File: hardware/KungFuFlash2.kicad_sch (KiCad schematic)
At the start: 52 parts, among them J1 SWD, J2 USB_B_Micro, J3 Wifi, Q1 BC817, SW1 Reset, SW2 Menu, SW3 Special, U1 C64-Exp-Port, U2 AMS1117-3.3, U3 STM32H7B0VBTx, Y1 25MHz

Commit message: Add USB C and JLCPCB files
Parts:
- removed J2: USB_B_Micro, KungFuFlash2:Conn_USBmicro-B_ebay-side_TH, symbol KungFuFlash2:USB_B_Micro-Connector
- removed Y1: 25MHz, Crystal:Crystal_SMD_5032-2Pin_5.0x3.2mm, symbol Device:Crystal
- added J4: USB_C_Receptacle_USB2.0, Connector_USB:USB_C_Receptacle_XKB_U262-16XN-4BVC11, symbol Connector:USB_C_Receptacle_USB2.0
- added R16, R17: 10k, Resistor_SMD:R_0805_2012Metric_Pad1.20x1.40mm_HandSolder, symbol Device:R
- added Y1: 25 MHz, Crystal:Crystal_SMD_3225-4Pin_3.2x2.5mm, symbol Device:Crystal_GND24
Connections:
- net +5C: now also J4.A4 (VBUS), J4.A9 (VBUS), J4.B4 (VBUS), J4.B9 (VBUS)
- net GND: now also J4.A1 (GND), J4.A12 (GND), J4.B1 (GND), J4.B12 (GND), J4.S1 (SHIELD), R16.1, R17.1, Y1.2, Y1.4
- net USB_DM: now also J4.A7 (D-), J4.B7 (D-)
- net USB_DP: now also J4.A6 (D+), J4.B6 (D+)
- net at C7.2, U3.12 (PH0): now also Y1.3
- net at C8.2, U3.13 (PH1): now also Y1.1
- new net: J4.B5 (CC2), R16.2
- new net: J4.A5 (CC1), R17.2
- no-connect marks 26 -> 25
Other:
- moved on the sheet: C7, C8

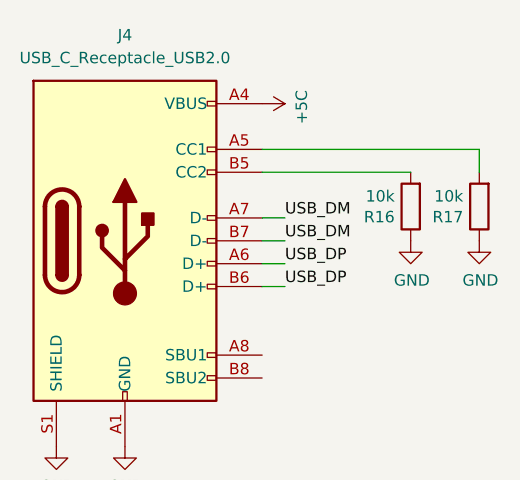
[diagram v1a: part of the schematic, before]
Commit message: Update PCB for USBC resistors 5.1k and production files
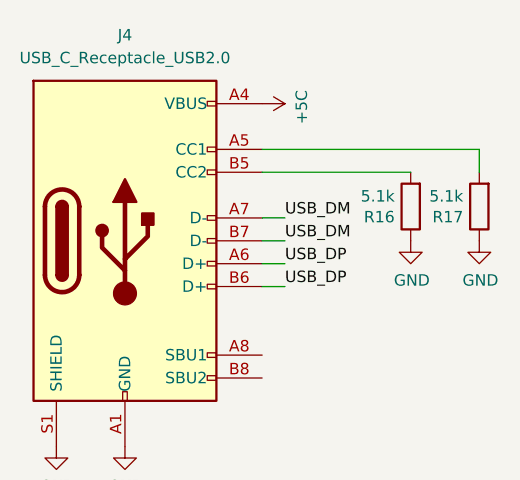
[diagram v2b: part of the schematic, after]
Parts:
- R16, R17: value 10k -> 5.1k
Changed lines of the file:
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@@
       (effects (font (size 1.27 1.27)) (justify left))
     )
-    (property "Value" "10k" (at 271.272 36.957 0)
+    (property "Value" "5.1k" (at 271.272 36.957 0)
       (effects (font (size 1.27 1.27)) (justify left))
     )
@@
       (effects (font (size 1.27 1.27)) (justify left))
     )
-    (property "Value" "10k" (at 278.892 36.957 0)
-      (effects (font (size 1.27 1.27)) (justify left))
-    )
+    (property "Value" "5.1k" (at 278.892 36.957 0)
+      (effects (font (size 1.27 1.27)) (justify left))
+    )

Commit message: SMT buttons
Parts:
- SW1, SW2, SW3: footprint Button_Switch_THT:SW_PUSH_6mm_H8mm -> Button_Switch_SMD:SW_SPST_PTS645
